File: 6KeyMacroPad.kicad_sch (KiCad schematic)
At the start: 39 parts, among them SW1 SW_Push, U1 ATmega32U4-A, Y1 16 MHz

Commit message: assign footprints
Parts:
- C1, C2, C3, C4, C5, C6, C7, C8: footprint (none) -> Capacitor_SMD:C_0805_2012Metric
- D1, D2, D3, D4, D5, D6: footprint (none) -> Diode_SMD:D_SOD-123
- F1: footprint (none) -> Fuse:Fuse_1206_3216Metric
- R1, R2, R3, R4, R5, R6, R7: footprint (none) -> Resistor_SMD:R_0805_2012Metric
- S1, S2, S3, S4, S5, S6: footprint (none) -> ScottoKeebs_Hotswap:Hotswap_MX_1.00u
- SW1: footprint (none) -> Button_Switch_SMD:SW_SPST_SKQG_WithStem
- USB1: footprint (none) -> Type-C:HRO-TYPE-C-31-M-12-HandSoldering
- Y1: footprint (none) -> Crystal:Crystal_SMD_3225-4Pin_3.2x2.5mm_HandSoldering
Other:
- title: (none) -> 6 Key Macropad 
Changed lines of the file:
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@@
 	(generator_version "8.0")
 	(paper "A4")
+	(title_block
+		(title "6 Key Macropad ")
+		(rev "V1")
+	)
 	(junction
 		(at 231.14 119.38)
@@
 			)
 		)
-		(property "Footprint" ""
+		(property "Footprint" "ScottoKeebs_Hotswap:Hotswap_MX_1.00u"
 			(at 228.6 109.22 0)
 			(effects
@@
 			)
 		)
-		(property "Footprint" ""
+		(property "Footprint" "Diode_SMD:D_SOD-123"
 			(at 201.93 115.57 0)
 			(effects
@@
 			)
 		)
-		(property "Footprint" ""
+		(property "Footprint" "Diode_SMD:D_SOD-123"
 			(at 231.14 115.57 0)
 			(effects
@@
 			)
 		)
-		(property "Footprint" ""
+		(property "Footprint" "Diode_SMD:D_SOD-123"
 			(at 217.17 115.57 0)
 			(effects
@@
 			)
 		)
-		(property "Footprint" ""
+		(property "Footprint" "Resistor_SMD:R_0805_2012Metric"
 			(at 72.39 120.65 0)
 			(effects
@@
 			)
 		)
-		(property "Footprint" ""
+		(property "Footprint" "Capacitor_SMD:C_0805_2012Metric"
 			(at 201.93 44.45 0)
 			(effects
@@
 			)
 		)
-		(property "Footprint" ""
+		(property "Footprint" "Capacitor_SMD:C_0805_2012Metric"
 			(at 190.5 44.45 0)
 			(effects
@@
 			)
 		)
-		(property "Footprint" ""
+		(property "Footprint" "Diode_SMD:D_SOD-123"
 			(at 201.93 96.52 0)
 			(effects
@@
 			)
 		)
-		(property "Footprint" ""
+		(property "Footprint" "Diode_SMD:D_SOD-123"
 			(at 217.17 96.52 0)
 			(effects
@@
 			)
 		)
-		(property "Footprint" ""
+		(property "Footprint" "Diode_SMD:D_SOD-123"
 			(at 231.14 96.52 0)
 			(effects
@@
 			)
 		)
-		(property "Footprint" ""
+		(property "Footprint" "ScottoKeebs_Hotswap:Hotswap_MX_1.00u"
 			(at 214.63 90.17 0)
 			(effects
@@
 			)
 		)
-		(property "Footprint" ""
+		(property "Footprint" "Resistor_SMD:R_0805_2012Metric"
 			(at 153.67 57.15 0)
 			(effects
@@
 			)
 		)
-		(property "Footprint" ""
+		(property "Footprint" "Capacitor_SMD:C_0805_2012Metric"
 			(at 74.93 63.5 0)
 			(effects
@@
 			)
 		)
-		(property "Footprint" ""
+		(property "Footprint" "Capacitor_SMD:C_0805_2012Metric"
 			(at 93.98 63.5 0)
 			(effects
@@
 			)
 		)
-		(property "Footprint" ""
+		(property "Footprint" "Fuse:Fuse_1206_3216Metric"
 			(at 83.82 96.52 0)
 			(effects
@@
 			)
 		)
-		(property "Footprint" ""
+		(property "Footprint" "Type-C:HRO-TYPE-C-31-M-12-HandSoldering"
 			(at 50.8 109.22 0)
 			(effects
@@
 			)
 		)
-		(property "Footprint" ""
+		(property "Footprint" "Resistor_SMD:R_0805_2012Metric"
 			(at 102.87 74.93 0)
 			(effects
@@
 			)
 		)
-		(property "Footprint" ""
+		(property "Footprint" "Crystal:Crystal_SMD_3225-4Pin_3.2x2.5mm_HandSoldering"
 			(at 85.09 59.69 0)
 			(effects
@@
 			)
 		)
-		(property "Footprint" ""
+		(property "Footprint" "Capacitor_SMD:C_0805_2012Metric"
 			(at 236.22 44.45 0)
 			(effects
@@
 			)
 		)
-		(property "Footprint" ""
+		(property "Footprint" "Resistor_SMD:R_0805_2012Metric"
 			(at 161.29 102.87 0)
 			(effects
@@
 			)
 		)
-		(property "Footprint" ""
+		(property "Footprint" "Resistor_SMD:R_0805_2012Metric"
 			(at 111.76 43.18 0)
 			(effects
@@
 			)
 		)
-		(property "Footprint" ""
+		(property "Footprint" "ScottoKeebs_Hotswap:Hotswap_MX_1.00u"
 			(at 228.6 90.17 0)
 			(effects
@@
 			)
 		)
-		(property "Footprint" ""
+		(property "Footprint" "ScottoKeebs_Hotswap:Hotswap_MX_1.00u"
 			(at 214.63 109.22 0)
 			(effects
@@
 			)
 		)
-		(property "Footprint" ""
+		(property "Footprint" "ScottoKeebs_Hotswap:Hotswap_MX_1.00u"
 			(at 199.39 109.22 0)
 			(effects
@@
 			)
 		)
-		(property "Footprint" ""
+		(property "Footprint" "Capacitor_SMD:C_0805_2012Metric"
 			(at 213.36 44.45 0)
 			(effects
@@
 			)
 		)
-		(property "Footprint" ""
+		(property "Footprint" "Resistor_SMD:R_0805_2012Metric"
 			(at 67.31 120.65 0)
 			(effects
@@
 			)
 		)
-		(property "Footprint" ""
+		(property "Footprint" "Resistor_SMD:R_0805_2012Metric"
 			(at 110.49 77.47 0)
 			(effects
@@
 			)
 		)
-		(property "Footprint" ""
+		(property "Footprint" "Button_Switch_SMD:SW_SPST_SKQG_WithStem"
 			(at 99.06 44.45 0)
 			(effects
@@
 			)
 		)
-		(property "Footprint" ""
+		(property "Footprint" "ScottoKeebs_Hotswap:Hotswap_MX_1.00u"
 			(at 199.39 90.17 0)
 			(effects
@@
 			)
 		)
-		(property "Footprint" ""
+		(property "Footprint" "Capacitor_SMD:C_0805_2012Metric"
 			(at 109.22 85.09 0)
 			(effects
@@
 			)
 		)
-		(property "Footprint" ""
+		(property "Footprint" "Capacitor_SMD:C_0805_2012Metric"
 			(at 224.79 44.45 0)
 			(effects

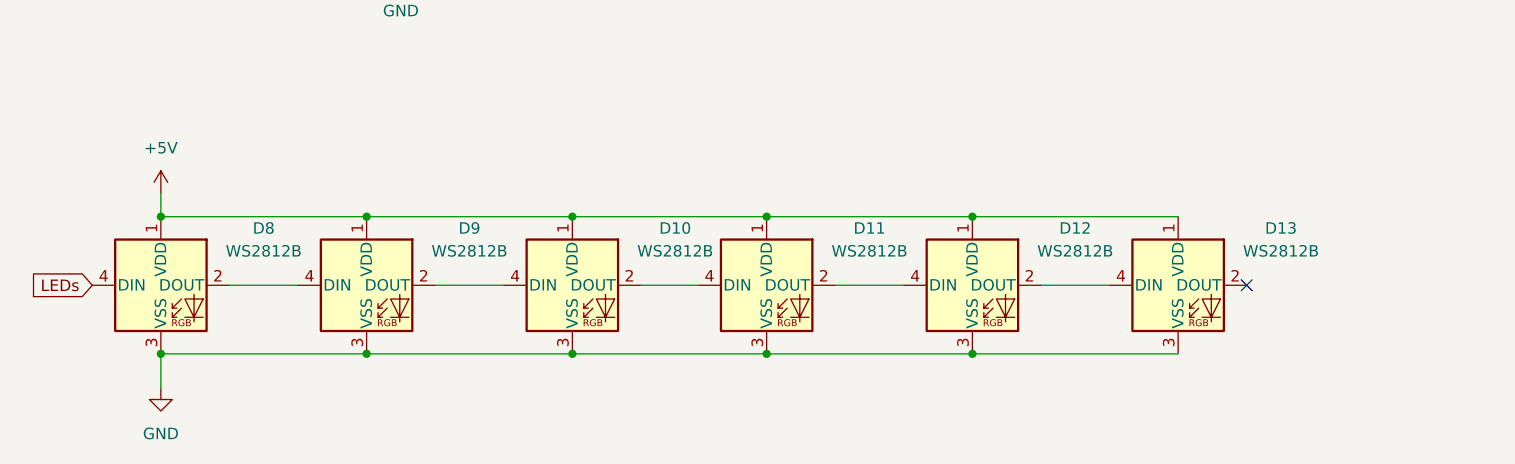
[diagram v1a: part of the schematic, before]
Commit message: board layout updates
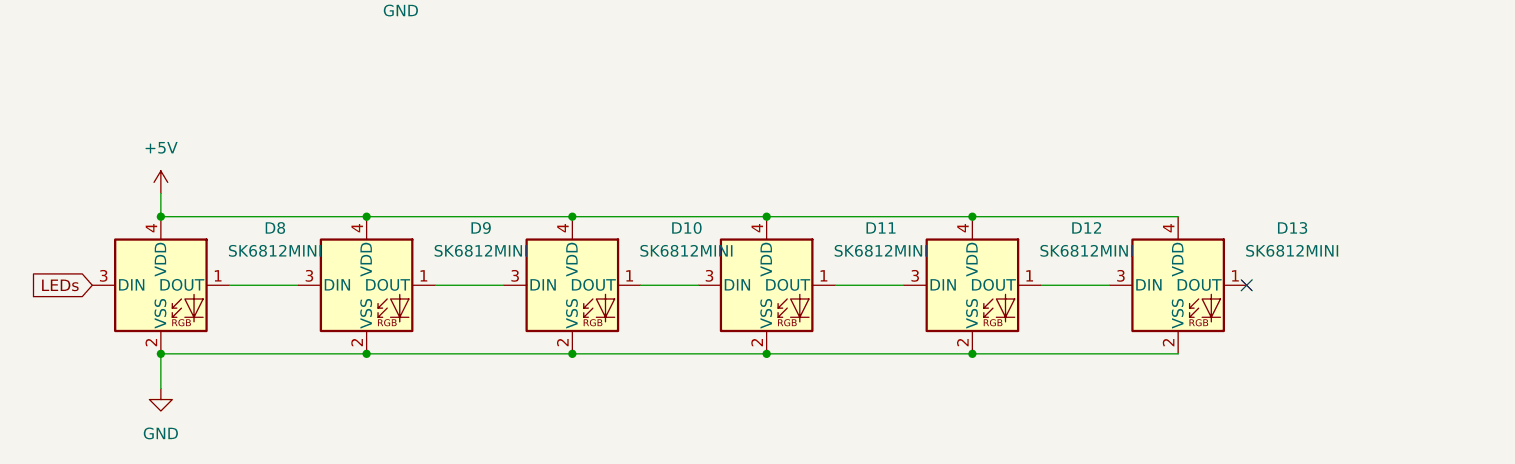
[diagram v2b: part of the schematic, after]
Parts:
- removed D10, D11, D12, D13, D8, D9: WS2812B, LED_SMD:LED_WS2812B_PLCC4_5.0x5.0mm_P3.2mm, symbol LED:WS2812B
- added D10, D11, D12, D13, D8, D9: SK6812MINI, kicad-keyboard-parts:MX_SK6812MINI-E, symbol LED:SK6812MINI
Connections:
- net +5V: now also D10.4 (VDD), D11.4 (VDD), D12.4 (VDD), D13.4 (VDD), D8.4 (VDD), D9.4 (VDD)
- net GND: now also D10.2 (VSS), D11.2 (VSS), D12.2 (VSS), D13.2 (VSS), D8.2 (VSS), D9.2 (VSS)
- net LEDs: now also D8.3 (DIN)
- new net: D12.1 (DOUT), D13.3 (DIN)
- new net: D11.1 (DOUT), D12.3 (DIN)
- new net: D8.1 (DOUT), D9.3 (DIN)
- new net: D10.1 (DOUT), D11.3 (DIN)
- new net: D10.3 (DIN), D9.1 (DOUT)

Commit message: footprint edits, routing updates
drc checked
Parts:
- removed U1: ATmega32U4-A, Package_QFP:TQFP-44_10x10mm_P0.8mm, symbol MCU_Microchip_ATmega:ATmega32U4-A
- added C10, C11, C12, C13, C9: 100 nF, Capacitor_SMD:C_0805_2012Metric, symbol Device:C_Small
- added FB1: 60@100MHz, Inductor_SMD:L_0805_2012Metric_Pad1.15x1.40mm_HandSolder, symbol Device:FerriteBead_Small
- added U2: ATmega32U2-A, Package_QFP:TQFP-32_7x7mm_P0.8mm, symbol MCU_Microchip_ATmega:ATmega32U2-A
- C7: value 0.1 uF -> 10 uF
- C8: value 10 uF -> 100 nF
- D10, D11, D12, D13, D8, D9: value SK6812MINI -> SK6812MINI-E
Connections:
- net +5V: now also C8.2, D10.1 (VDD), D11.1 (VDD), D12.1 (VDD), D13.1 (VDD), D8.1 (VDD), D9.1 (VDD), C10.2, C11.2, C12.2, C13.2, C9.2, U2.31 (UVCC), U2.32 (AVCC), U2.4 (VCC); no longer C8.1, D10.4 (VDD), D11.4 (VDD), D12.4 (VDD), D13.4 (VDD), D8.4 (VDD), D9.4 (VDD)
- net Column 0: now also U2.10 (PD4)
- net Column 1: now also U2.8 (PD2)
- net Column 2: now also U2.9 (PD3)
- net GND: now also C8.1, D10.3 (VSS), D11.3 (VSS), D12.3 (VSS), D13.3 (VSS), D8.3 (VSS), D9.3 (VSS), C10.1, C11.1, C12.1, C13.1, C9.1, FB1.2, U2.28 (UGND), U2.3 (GND); no longer C8.2, D10.2 (VSS), D11.2 (VSS), D12.2 (VSS), D13.2 (VSS), D8.2 (VSS), D9.2 (VSS), USB1.13 (SHIELD)
- net Row 0: now also U2.6 (PD0)
- net Row 1: now also U2.7 (PD1)
- net at R7.2: now also U2.5 (PC2)
- net at C1.1, Y1.1: now also U2.1 (XTAL1)
- net at C2.1, Y1.3: now also U2.2 (PC0/XTAL2)
- net at R1.2: now also U2.29 (D+)
- net at R4.1: now also U2.13 (~{HWB}/PD7)
- net at R3.2, SW1.2: now also U2.24 (PC1/~{RESET})
- net at R2.2: now also U2.30 (D-)
- net at C3.1: now also U2.27 (UCAP)
- net LEDs renamed D1
- net D1: now also D13.4 (DIN); no longer D8.3 (DIN)
- new net: D11.4 (DIN), D12.2 (DOUT)
- new net: D12.4 (DIN), D13.2 (DOUT)
- new net: D10.2 (DOUT), D9.4 (DIN)
- new net: D10.4 (DIN), D11.2 (DOUT)
- new net: D8.4 (DIN), D9.2 (DOUT)
- new net Earth: FB1.1, USB1.13 (SHIELD)
- no-connect marks 23 -> 17
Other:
- moved on the sheet: C1, C2, C3, C4, C5, C6, C7, D1, D2, D3, D4, D5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

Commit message: manufacturing files changed
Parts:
- R7: value 500 -> 300
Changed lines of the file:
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@@
 			)
 		)
-		(property "Value" "500"
+		(property "Value" "300"
 			(at 158.75 76.962 90)
 			(effects
